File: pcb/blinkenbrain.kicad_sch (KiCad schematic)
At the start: 29 parts, among them Q1 BC847BS, Q2 NX6008NBKW, SW1 DS04-254-2-01BK-SMT, U1 TPS613222ADBVR

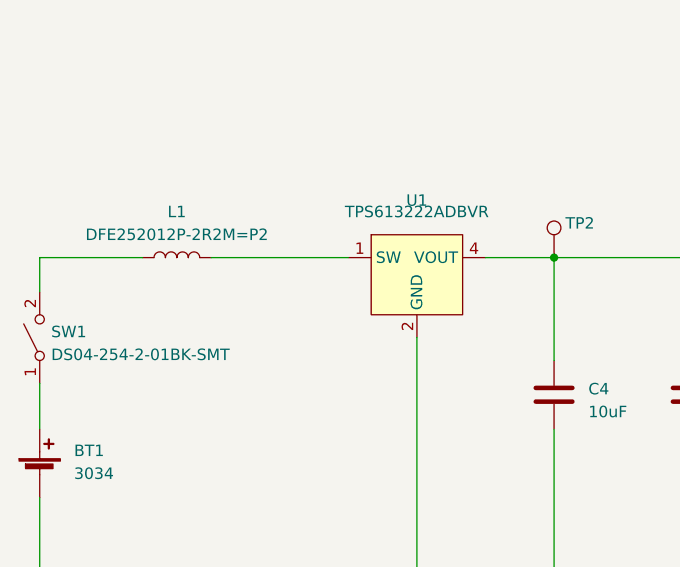
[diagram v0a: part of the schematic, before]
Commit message: Rev. B
- Small changes after testing (completely functional but some foot
prints were a bit off)
- Changed DIP switch so that its easier to actuate
- Created 20 peice panel
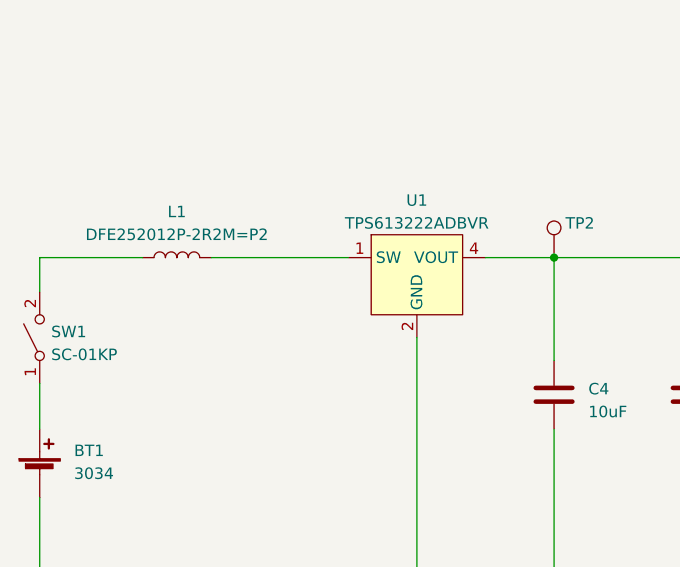
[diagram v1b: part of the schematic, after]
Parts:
- BT1: footprint Battery:BatteryHolder_Keystone_3034_1x20mm -> open-ephys:KEYSTONE_3034_1x20mm
- Q2: footprint Package_TO_SOT_SMD:SOT-23-3 -> Package_TO_SOT_SMD:SOT-323_SC-70
- SW1: value DS04-254-2-01BK-SMT -> SC-01KP; footprint Button_Switch_SMD:SW_DIP_SPSTx01_Slide_6.7x4.1mm_W8.61mm_P2.54mm_LowProfile -> open-ephys:DEALON_DIP_SPSTx01_SC-01KP_W7.62mm_P1.27mm
- U1: value TPS613222ADBVR -> TPS613222ADBVR
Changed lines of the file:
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@@
   (title_block
     (title "Blinkenbrain")
-    (rev "A")
+    (rev "B")
     (company "Open Ephys, Inc")
     (comment 1 "Jonathan P. Newman")
@@
       (effects (font (size 1.27 1.27)))
     )
-    (property "Value" "	\nTPS613222ADBVR" (at 67.31 59.69 0)
+    (property "Value" "TPS613222ADBVR" (at 67.31 60.96 0)
       (effects (font (size 1.27 1.27)))
     )
@@
       (effects (font (size 1.27 1.27)) (justify left))
     )
-    (property "Footprint" "Battery:BatteryHolder_Keystone_3034_1x20mm" (at 25.4 87.376 90)
-      (effects (font (size 1.27 1.27)) hide)
-    )
-    (property "Datasheet" "~" (at 25.4 87.376 90)
+    (property "Footprint" "open-ephys:KEYSTONE_3034_1x20mm" (at 25.4 87.376 90)
+      (effects (font (size 1.27 1.27)) hide)
+    )
+    (property "Datasheet" "https://www.keyelco.com/userAssets/file/M65p9.pdf" (at 25.4 87.376 90)
       (effects (font (size 1.27 1.27)) hide)
     )
@@
       (effects (font (size 1.27 1.27)) (justify right))
     )
-    (property "Value" "DS04-254-2-01BK-SMT" (at 26.67 75.565 90)
+    (property "Value" "SC-01KP" (at 26.67 75.565 90)
       (effects (font (size 1.27 1.27)) (justify right))
     )
-    (property "Footprint" "Button_Switch_SMD:SW_DIP_SPSTx01_Slide_6.7x4.1mm_W8.61mm_P2.54mm_LowProfile" (at 25.4 73.66 0)
+    (property "Footprint" "open-ephys:DEALON_DIP_SPSTx01_SC-01KP_W7.62mm_P1.27mm" (at 25.4 73.66 0)
       (effects (font (size 1.27 1.27)) hide)
     )
@@
       (effects (font (size 1.27 1.27)) (justify left))
     )
-    (property "Footprint" "Package_TO_SOT_SMD:SOT-23-3" (at 252.73 133.985 0)
+    (property "Footprint" "Package_TO_SOT_SMD:SOT-323_SC-70" (at 252.73 133.985 0)
       (effects (font (size 1.27 1.27) italic) (justify left) hide)
     )
